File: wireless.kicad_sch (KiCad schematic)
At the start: 37 parts, among them J1301 u.FL, U1301 LBEE5KL1YN-814

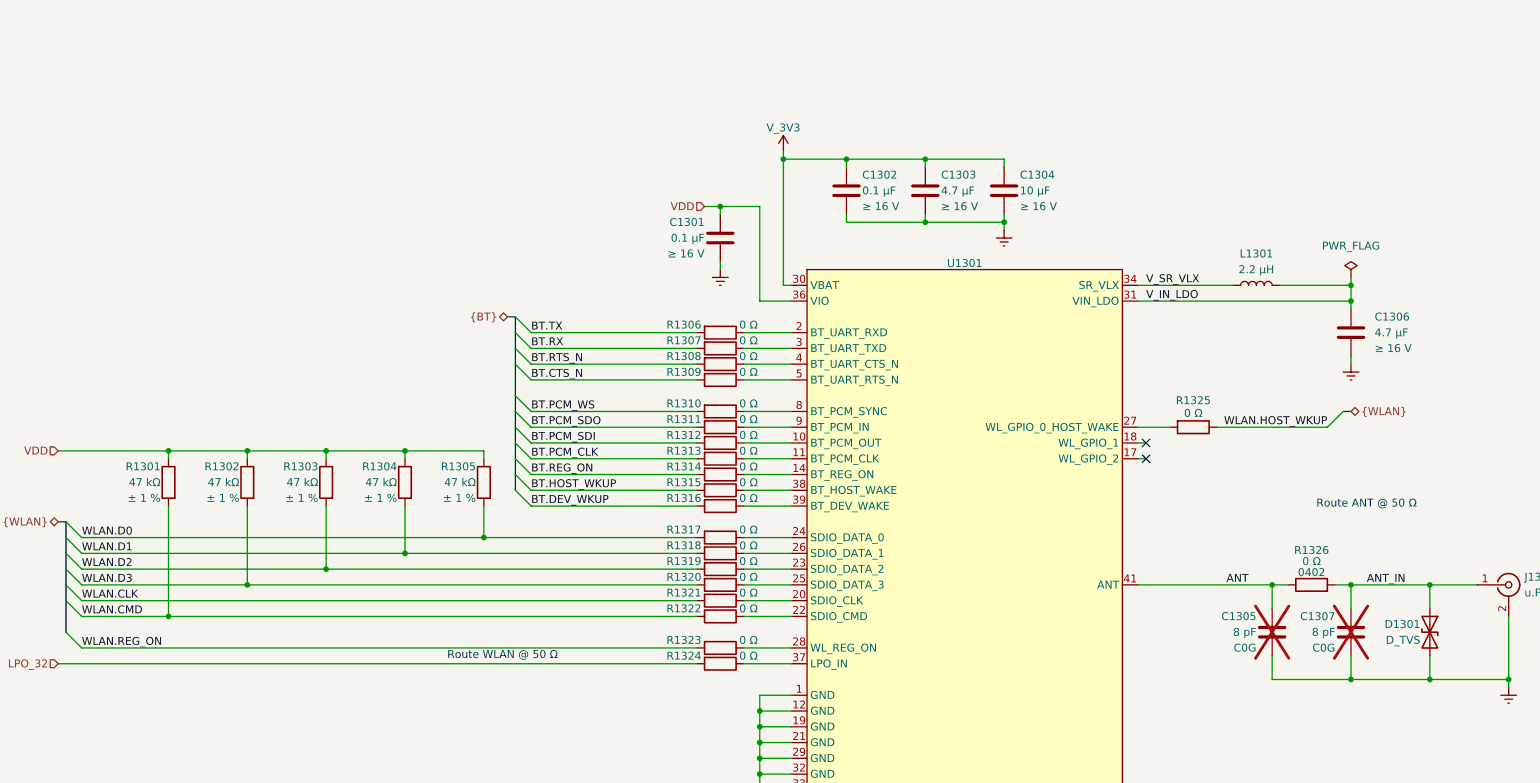
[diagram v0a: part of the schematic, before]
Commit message: Add additional info to passives
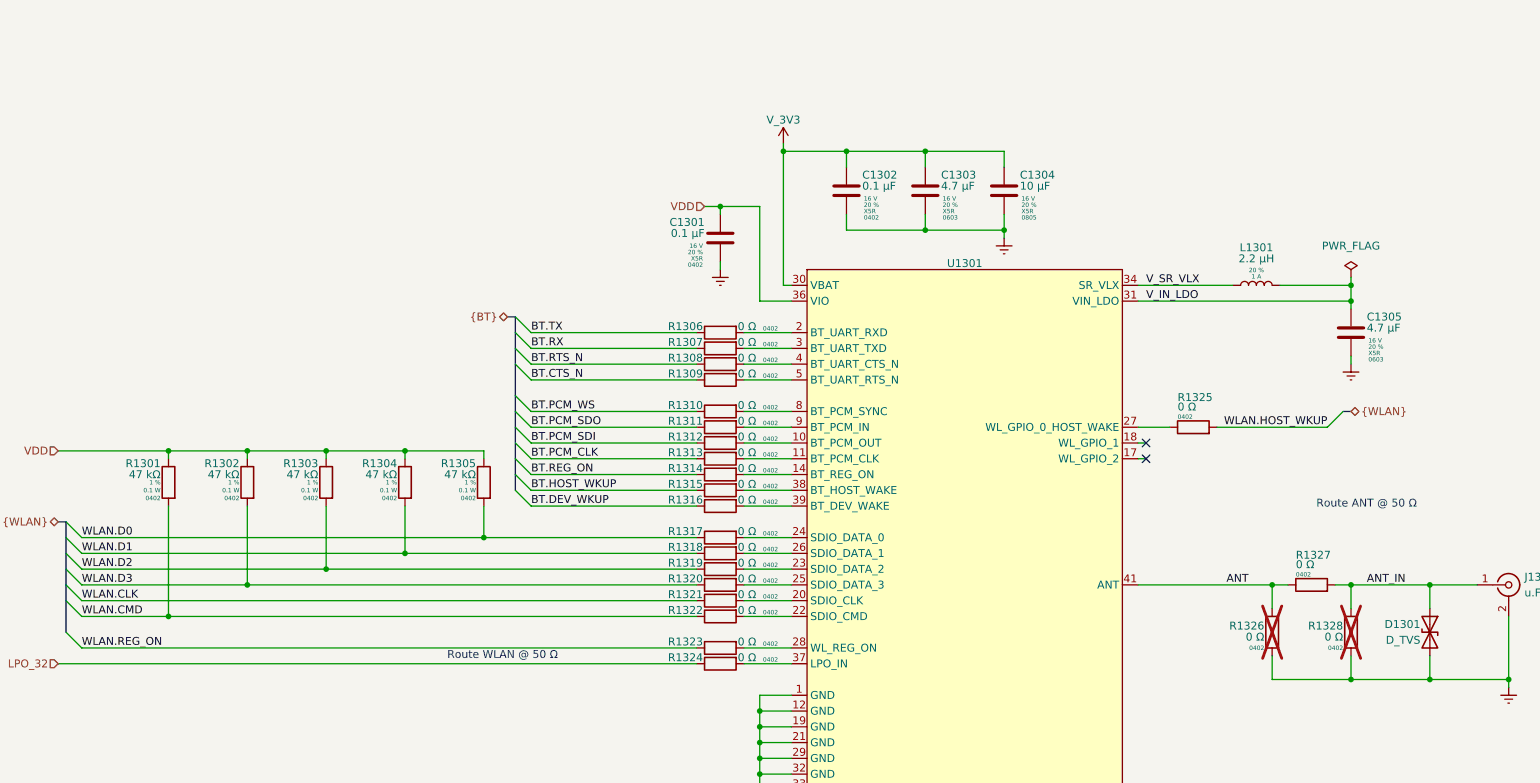
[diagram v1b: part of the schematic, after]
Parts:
- removed C1306: 4.7 µF, Capacitor_SMD:C_0603_1608Metric, symbol Device:C
- removed C1307: 8 pF, symbol Device:C
- added R1327, R1328: 0 Ω, symbol Device:R
- C1301, C1302: Size (none) -> 0402; Temperature coefficient (none) -> X5R; Tolerance (none) -> 20 %; Voltage rating ≥ 16 V -> 16 V
- C1303: footprint Capacitor_SMD:C_0603_1608Metric -> (none); MPN GRM188R6YA475KE15D -> (none); Manufacturer Murata Electronics -> (none); Size (none) -> 0603; Temperature coefficient (none) -> X5R; Tolerance (none) -> 20 %; Voltage rating ≥ 16 V -> 16 V
- C1304: Size (none) -> 0805; Temperature coefficient (none) -> X5R; Tolerance (none) -> 20 %; Voltage rating ≥ 16 V -> 16 V
- C1305: value 8 pF -> 4.7 µF; Size (none) -> 0603; Temperature coefficient C0G -> X5R; Tolerance (none) -> 20 %; Voltage rating (none) -> 16 V; now fitted
- L1301: Current rating (none) -> 1 A; Tolerance (none) -> 20 %
- R1301, R1302, R1303, R1304, R1305: Power rating (none) -> 0.1 W; Size (none) -> 0402; Tolerance ± 1 % -> 1 %
- R1306, R1307, R1308, R1309, R1310, R1311, R1312, R1313, R1314, R1315, R1316, R1317, R1318, R1319, R1320, R1321, R1322, R1323, R1324, R1325: footprint perfect_footprints:R_0402_1005Metric -> (none); MPN 560112110020 -> (none); Manufacturer Würth Elektronik -> (none); Size (none) -> 0402
- R1326: now not fitted; now left out of the parts list
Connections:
- net ANT: now also R1327.1; no longer C1305.1
- net ANT_IN: now also R1327.2, R1328.1; no longer R1326.2
- net BT.CTS_N: now also R1309.1; no longer R1309.2
- net BT.DEV_WKUP: now also R1316.1; no longer R1316.2
- net BT.HOST_WKUP: now also R1315.1; no longer R1315.2
- net BT.PCM_CLK: now also R1313.1; no longer R1313.2
- net BT.PCM_SDI: now also R1312.1; no longer R1312.2
- net BT.PCM_SDO: now also R1311.1; no longer R1311.2
- net BT.PCM_WS: now also R1310.1; no longer R1310.2
- net BT.REG_ON: now also R1314.1; no longer R1314.2
- net BT.RTS_N: now also R1308.1; no longer R1308.2
- net BT.RX: now also R1307.1; no longer R1307.2
- net BT.TX: now also R1306.1; no longer R1306.2
- net GND: now also R1326.2, R1328.2
- net LPO_32: now also R1324.1; no longer R1324.2
- net V_IN_LDO: now also C1305.1
- net WLAN.CLK: now also R1321.1; no longer R1321.2
- net WLAN.CMD: now also R1322.1; no longer R1322.2
- net WLAN.D0: now also R1317.1; no longer R1317.2
- net WLAN.D1: now also R1318.1; no longer R1318.2
- net WLAN.D2: now also R1319.1; no longer R1319.2
- net WLAN.D3: now also R1320.1; no longer R1320.2
- net WLAN.HOST_WKUP: now also R1325.2; no longer R1325.1
- net WLAN.REG_ON: now also R1323.1; no longer R1323.2
- net at U1301.24 (SDIO_DATA_0): now also R1317.2; no longer R1317.1
- net at U1301.4 (BT_UART_CTS_N): now also R1308.2; no longer R1308.1
- net at U1301.39 (BT_DEV_WAKE): now also R1316.2; no longer R1316.1
- net at U1301.28 (WL_REG_ON): now also R1323.2; no longer R1323.1
- net at U1301.5 (BT_UART_RTS_N): now also R1309.2; no longer R1309.1
- net at U1301.10 (BT_PCM_OUT): now also R1312.2; no longer R1312.1
- net at U1301.11 (BT_PCM_CLK): now also R1313.2; no longer R1313.1
- net at U1301.14 (BT_REG_ON): now also R1314.2; no longer R1314.1
- net at U1301.2 (BT_UART_RXD): now also R1306.2; no longer R1306.1
- net at U1301.20 (SDIO_CLK): now also R1321.2; no longer R1321.1
- net at U1301.22 (SDIO_CMD): now also R1322.2; no longer R1322.1
- net at U1301.23 (SDIO_DATA_2): now also R1319.2; no longer R1319.1
- net at U1301.25 (SDIO_DATA_3): now also R1320.2; no longer R1320.1
- net at U1301.26 (SDIO_DATA_1): now also R1318.2; no longer R1318.1
- net at U1301.27 (WL_GPIO_0_HOST_WAKE): now also R1325.1; no longer R1325.2
- net at U1301.3 (BT_UART_TXD): now also R1307.2; no longer R1307.1
- net at U1301.37 (LPO_IN): now also R1324.2; no longer R1324.1
- net at U1301.38 (BT_HOST_WAKE): now also R1315.2; no longer R1315.1
- net at U1301.8 (BT_PCM_SYNC): now also R1310.2; no longer R1310.1
- net at U1301.9 (BT_PCM_IN): now also R1311.2; no longer R1311.1

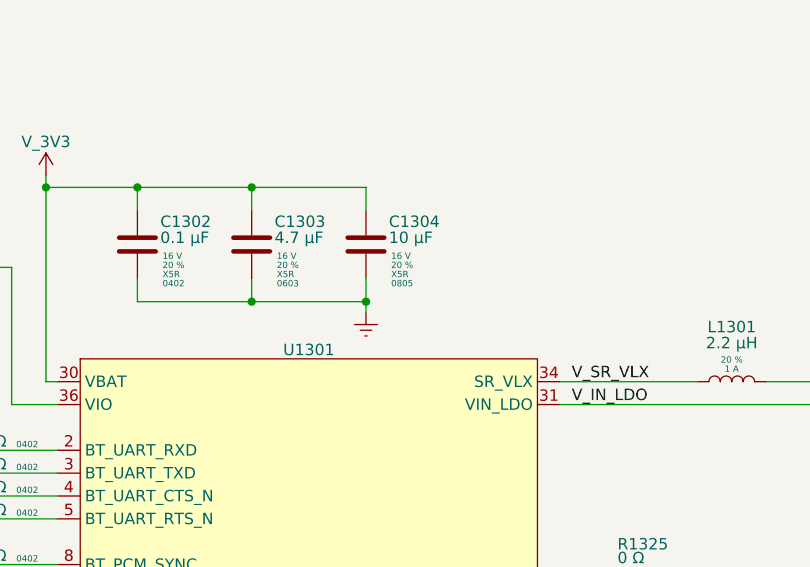
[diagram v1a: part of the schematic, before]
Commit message: Update capacitor BOM
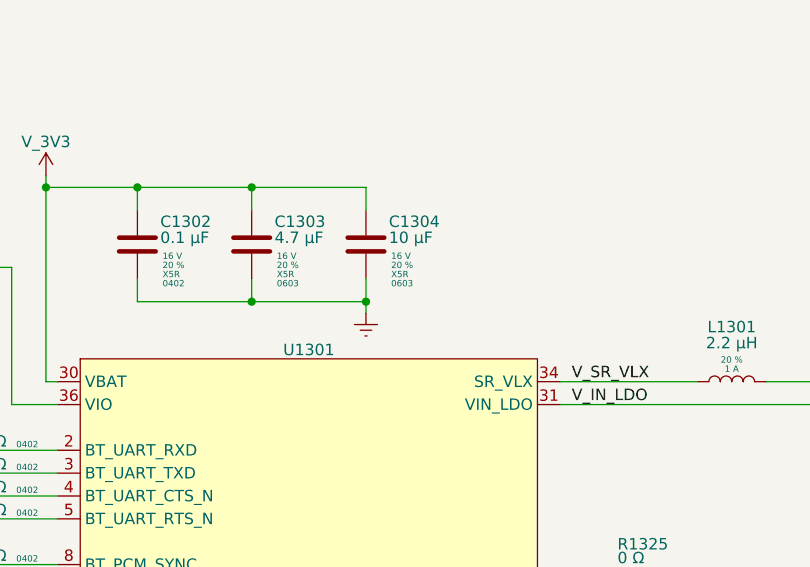
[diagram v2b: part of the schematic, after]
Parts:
- C1301, C1302: footprint (none) -> perfect_footprints:C_0402_1005Metric; Digi-Key Part Number (none) -> 490-10700-1-ND; MPN (none) -> GRM155R71H104KE14D; Manufacturer (none) -> Murata Electronics
- C1303, C1305: footprint (none) -> Capacitor_SMD:C_0603_1608Metric; Digi-Key Part Number (none) -> 490-7205-1-ND; MPN (none) -> GRM188R6YA475KE15D; Manufacturer (none) -> Murata Electronics
- C1304: footprint (none) -> Capacitor_SMD:C_0603_1608Metric; Digi-Key Part Number (none) -> 490-13248-1-ND; MPN (none) -> GRM188R6YA106MA73D; Manufacturer (none) -> Murata Electronics; Size 0805 -> 0603
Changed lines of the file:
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@@
 			)
 		)
-		(property "Footprint" ""
+		(property "Footprint" "perfect_footprints:C_0402_1005Metric"
 			(at 199.0852 115.57 0)
 			(effects
@@
 			)
 		)
-		(property "Datasheet" ""
+		(property "Datasheet" "https://search.murata.co.jp/Ceramy/image/img/A01X/G101/ENG/GRM155R71H104KE14-01.pdf"
 			(at 198.12 111.76 0)
 			(effects
@@
 			)
 		)
-		(property "Description" ""
+		(property "Description" "0.1 µF ±10% 50V Ceramic Capacitor X7R 0402 (1005 Metric)"
 			(at 198.12 111.76 0)
 			(effects
@@
 			)
 		)
-		(property "MPN" ""
+		(property "MPN" "GRM155R71H104KE14D"
 			(at 198.12 111.76 0)
 			(effects
@@
 			)
 		)
-		(property "Manufacturer" ""
+		(property "Manufacturer" "Murata Electronics"
 			(at 198.12 111.76 0)
 			(effects
@@
 				)
 				(justify left)
+			)
+		)
+		(property "Digi-Key Part Number" "490-10700-1-ND"
+			(at 198.12 111.76 0)
+			(effects
+				(font
+					(size 1.27 1.27)
+				)
+				(hide yes)
 			)
 		)
@@
 			)
 		)
-		(property "Footprint" ""
+		(property "Footprint" "Capacitor_SMD:C_0603_1608Metric"
 			(at 211.7852 115.57 0)
 			(effects
@@
 			)
 		)
-		(property "Datasheet" "https://mm.digikey.com/Volume0/opasdata/d220001/medias/docus/609/CL21B105KBFNNNE_Spec.pdf"
+		(property "Datasheet" "https://search.murata.co.jp/Ceramy/image/img/A01X/G101/ENG/GRM188R6YA475KE15-01.pdf"
 			(at 210.82 111.76 0)
 			(effects
@@
 			)
 		)
-		(property "Description" "1 µF ±10% 50V Ceramic Capacitor X7R 0805 (2012 Metric)"
+		(property "Description" "4.7 µF ±10% 35V Ceramic Capacitor X5R 0603 (1608 Metric)"
 			(at 210.82 111.76 0)
 			(effects
@@
 			)
 		)
-		(property "MPN" ""
+		(property "MPN" "GRM188R6YA475KE15D"
 			(at 210.82 111.76 0)
 			(effects
@@
 			)
 		)
-		(property "Manufacturer" ""
+		(property "Manufacturer" "Murata Electronics"
 			(at 210.82 111.76 0)
 			(effects
@@
 				)
 				(justify left)
+			)
+		)
+		(property "Digi-Key Part Number" "490-7205-1-ND"
+			(at 210.82 111.76 0)
+			(effects
+				(font
+					(size 1.27 1.27)
+				)
+				(hide yes)
 			)
 		)
@@
 			)
 		)
-		(property "Footprint" ""
+		(property "Footprint" "Capacitor_SMD:C_0603_1608Metric"
 			(at 280.3652 138.43 0)
 			(effects
@@
 			)
 		)
-		(property "Datasheet" "https://mm.digikey.com/Volume0/opasdata/d220001/medias/docus/609/CL21B105KBFNNNE_Spec.pdf"
+		(property "Datasheet" "https://search.murata.co.jp/Ceramy/image/img/A01X/G101/ENG/GRM188R6YA475KE15-01.pdf"
 			(at 279.4 134.62 0)
 			(effects
@@
 			)
 		)
-		(property "Description" "1 µF ±10% 50V Ceramic Capacitor X7R 0805 (2012 Metric)"
+		(property "Description" "4.7 µF ±10% 35V Ceramic Capacitor X5R 0603 (1608 Metric)"
 			(at 279.4 134.62 0)
 			(effects
@@
 			)
 		)
-		(property "MPN" ""
+		(property "MPN" "GRM188R6YA475KE15D"
 			(at 279.4 134.62 0)
 			(effects
@@
 			)
 		)
-		(property "Manufacturer" ""
+		(property "Manufacturer" "Murata Electronics"
 			(at 279.4 134.62 0)
 			(effects
@@
 				)
 				(justify left)
+			)
+		)
+		(property "Digi-Key Part Number" "490-7205-1-ND"
+			(at 279.4 134.62 0)
+			(effects
+				(font
+					(size 1.27 1.27)
+				)
+				(hide yes)
 			)
 		)
@@
 			)
 		)
-		(property "Footprint" ""
+		(property "Footprint" "perfect_footprints:C_0402_1005Metric"
 			(at 176.8348 123.19 0)
 			(effects
@@
 			)
 		)
-		(property "Datasheet" ""
+		(property "Datasheet" "https://search.murata.co.jp/Ceramy/image/img/A01X/G101/ENG/GRM155R71H104KE14-01.pdf"
 			(at 177.8 119.38 0)
 			(effects
@@
 			)
 		)
-		(property "Description" ""
+		(property "Description" "0.1 µF ±10% 50V Ceramic Capacitor X7R 0402 (1005 Metric)"
 			(at 177.8 119.38 0)
 			(effects
@@
 			)
 		)
-		(property "MPN" ""
+		(property "MPN" "GRM155R71H104KE14D"
 			(at 177.8 119.38 0)
 			(effects
@@
 			)
 		)
-		(property "Manufacturer" ""
+		(property "Manufacturer" "Murata Electronics"
 			(at 177.8 119.38 0)
 			(effects
@@
 				)
 				(justify left)
+			)
+		)
+		(property "Digi-Key Part Number" "490-10700-1-ND"
+			(at 177.8 119.38 0)
+			(effects
+				(font
+					(size 1.27 1.27)
+				)
+				(hide yes)
 			)
 		)
@@
 			)
 		)
-		(property "Footprint" ""
+		(property "Footprint" "Capacitor_SMD:C_0603_1608Metric"
 			(at 224.4852 115.57 0)
 			(effects
@@
 			)
 		)
-		(property "Datasheet" ""
+		(property "Datasheet" "https://search.murata.co.jp/Ceramy/image/img/A01X/G101/ENG/GRM188R6YA106MA73-01A.pdf"
 			(at 223.52 111.76 0)
 			(effects
@@
 			)
 		)
-		(property "Description" ""
+		(property "Description" "10 µF ±20% 35V Ceramic Capacitor X5R 0603 (1608 Metric)"
 			(at 223.52 111.76 0)
 			(effects
@@
 			)
 		)
-		(property "MPN" ""
+		(property "MPN" "GRM188R6YA106MA73D"
 			(at 223.52 111.76 0)
 			(effects
@@
 			)
 		)
-		(property "Manufacturer" ""
+		(property "Manufacturer" "Murata Electronics"
 			(at 223.52 111.76 0)
 			(effects
@@
 			)
 		)
-		(property "Size" "0805"
+		(property "Size" "0603"
 			(at 226.314 116.078 0)
 			(effects
@@
 			)
 		)
+		(property "Digi-Key Part Number" "490-13248-1-ND"
+			(at 223.52 111.76 0)
+			(effects
+				(font
+					(size 1.27 1.27)
+				)
+				(hide yes)
+			)
+		)

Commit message: Update R & L BOM
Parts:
- R1301, R1302, R1303, R1304, R1305: Digi-Key Part Number (none) -> P47.0KLCT-ND; MPN (none) -> ERJ-2RKF4702X; Manufacturer (none) -> Panasonic Electronic Components
- R1306, R1307, R1308, R1309, R1310, R1311, R1312, R1313, R1314, R1315, R1316, R1317, R1318, R1319, R1320, R1321, R1322, R1323, R1324, R1325, R1326, R1327, R1328: footprint (none) -> perfect_footprints:R_0402_1005Metric; Digi-Key Part Number (none) -> P0.0JCT-ND; MPN (none) -> ERJ-2GE0R00X; Manufacturer (none) -> Panasonic Electronic Components

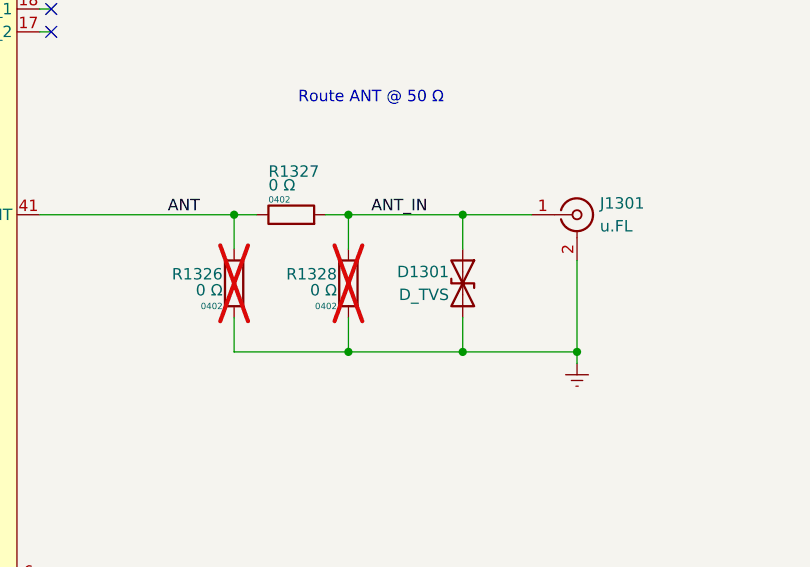
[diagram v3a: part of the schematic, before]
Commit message: Fill BOM info
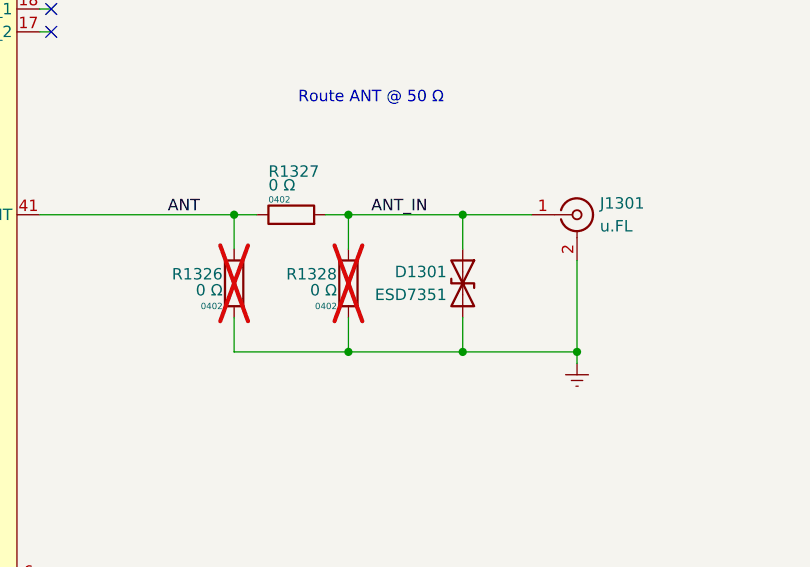
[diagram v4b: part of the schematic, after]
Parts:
- D1301: value D_TVS -> ESD7351; footprint (none) -> Diode_SMD:D_SOD-323; Digi-Key Part Number (none) -> ESD7351HT1GOSCT-ND; MPN (none) -> ESD7351HT1G; Manufacturer (none) -> onsemi
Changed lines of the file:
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@@
-	)
-	(symbol
-		(lib_id "Device:D_TVS")
-		(at 292.1 182.88 270)
-		(unit 1)
-		(exclude_from_sim no)
-		(in_bom yes)
-		(on_board yes)
-		(dnp no)
-		(property "Reference" "D1301"
-			(at 290.576 181.61 90)
-			(effects
-				(font
-					(size 1.27 1.27)
-				)
-				(justify right)
-			)
-		)
-		(property "Value" "D_TVS"
-			(at 290.576 184.15 90)
-			(effects
-				(font
-					(size 1.27 1.27)
-				)
-				(justify right)
-			)
-		)
-		(property "Footprint" ""
-			(at 292.1 182.88 0)
-			(effects
-				(font
-					(size 1.27 1.27)
-				)
-				(hide yes)
-			)
-		)
-		(property "Datasheet" "~"
-			(at 292.1 182.88 0)
-			(effects
-				(font
-					(size 1.27 1.27)
-				)
-				(hide yes)
-			)
-		)
-		(property "Description" "Bidirectional transient-voltage-suppression diode"
-			(at 292.1 182.88 0)
-			(effects
-				(font
-					(size 1.27 1.27)
-				)
-				(hide yes)
-			)
-		)
-		(pin "1"
-		)
-		(pin "2"
-		)
-		(instances
-			(project "linux-sbc"
-				(path "/fa11a02f-8043-4153-ab69-88d766503017/24c9b83b-271d-4c51-b843-406c618d8ce8"
-					(reference "D1301")
-					(unit 1)
-				)
-			)
-		)
 	)
 	(symbol
@@
 					(unit 1)
 				)
+			)
+		)
+	)
+	(symbol
+		(lib_id "Device:D_TVS")
+		(at 292.1 182.88 270)
+		(unit 1)
+		(exclude_from_sim no)
+		(in_bom yes)
+		(on_board yes)
+		(dnp no)
+		(property "Reference" "D1301"
+			(at 290.322 181.61 90)
+			(effects
+				(font
+					(size 1.27 1.27)
+				)
+				(justify right)
+			)
+		)
+		(property "Value" "ESD7351"
+			(at 290.322 184.15 90)
+			(effects
+				(font
+					(size 1.27 1.27)
+				)
+				(justify right)
+			)
+		)
+		(property "Footprint" "Diode_SMD:D_SOD-323"
+			(at 292.1 182.88 0)
+			(effects
+				(font
+					(size 1.27 1.27)
+				)
+				(hide yes)
+			)
+		)
+		(property "Datasheet" "https://www.onsemi.com/pdf/datasheet/esd7351-d.pdf"
+			(at 292.1 182.88 0)
+			(effects
+				(font
+					(size 1.27 1.27)
+				)
+				(hide yes)
+			)
+		)
+		(property "Description" "Clamp Ipp Tvs Diode Surface Mount SOD-323"
+			(at 292.1 182.88 0)
+			(effects
+				(font
+					(size 1.27 1.27)
+				)
+				(hide yes)
+			)
+		)
+		(property "Digi-Key Part Number" "ESD7351HT1GOSCT-ND"
+			(at 292.1 182.88 90)
+			(effects
+				(font
+					(size 1.27 1.27)
+				)
+				(hide yes)
+			)
+		)
+		(property "MPN" "ESD7351HT1G"
+			(at 292.1 182.88 90)
+			(effects
+				(font
+					(size 1.27 1.27)
+				)
+				(hide yes)
+			)
+		)
+		(property "Manufacturer" "onsemi"
+			(at 292.1 182.88 90)
+			(effects
+				(font
+					(size 1.27 1.27)
+				)
+				(hide yes)
+			)
+		)
+		(pin "2"
+		)
+		(pin "1"
+		)
+		(instances
+			(project ""
+				(path "/fa11a02f-8043-4153-ab69-88d766503017/24c9b83b-271d-4c51-b843-406c618d8ce8"
+					(reference "D1301")
+					(unit 1)
+				)
